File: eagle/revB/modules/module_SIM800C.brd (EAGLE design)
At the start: 24.1 x 32.8 mm, 10 parts, among them IC1 SIM800C, X1 734120110

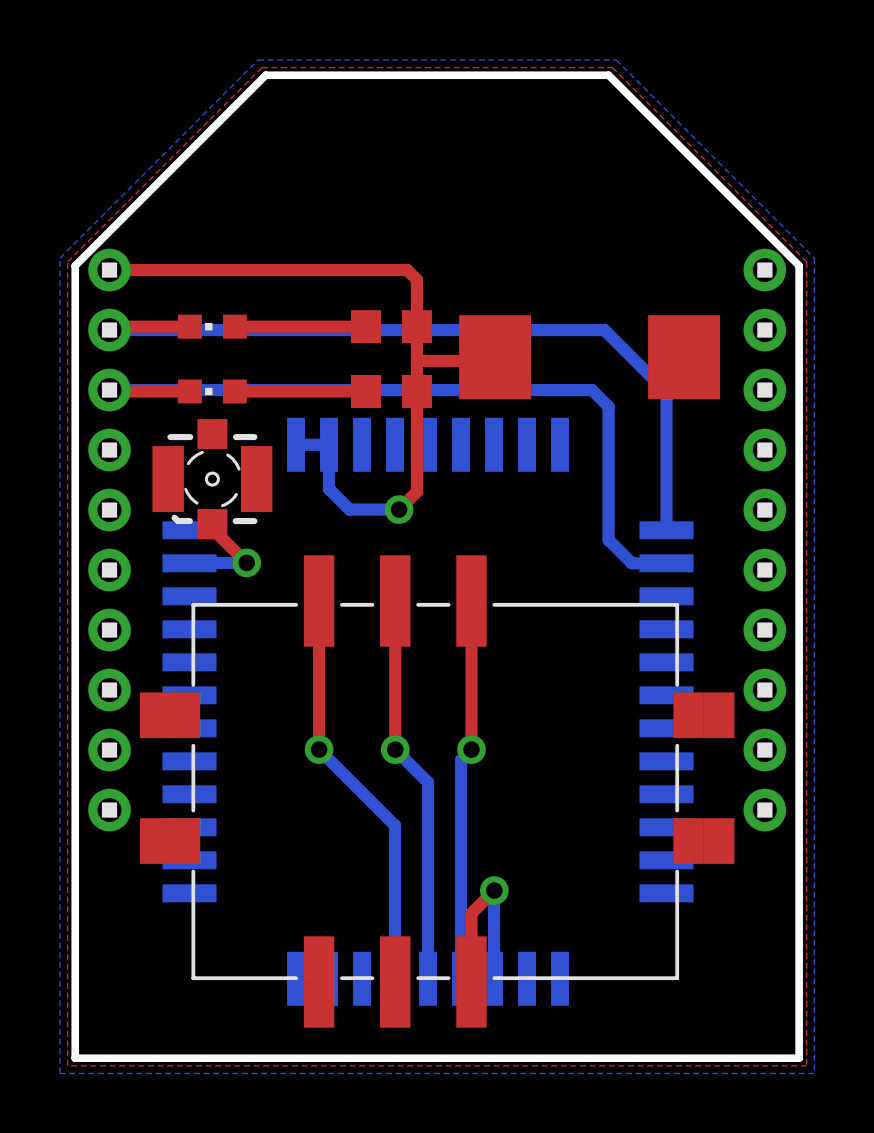
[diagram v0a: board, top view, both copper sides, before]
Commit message: [SIM800C] Updated layout
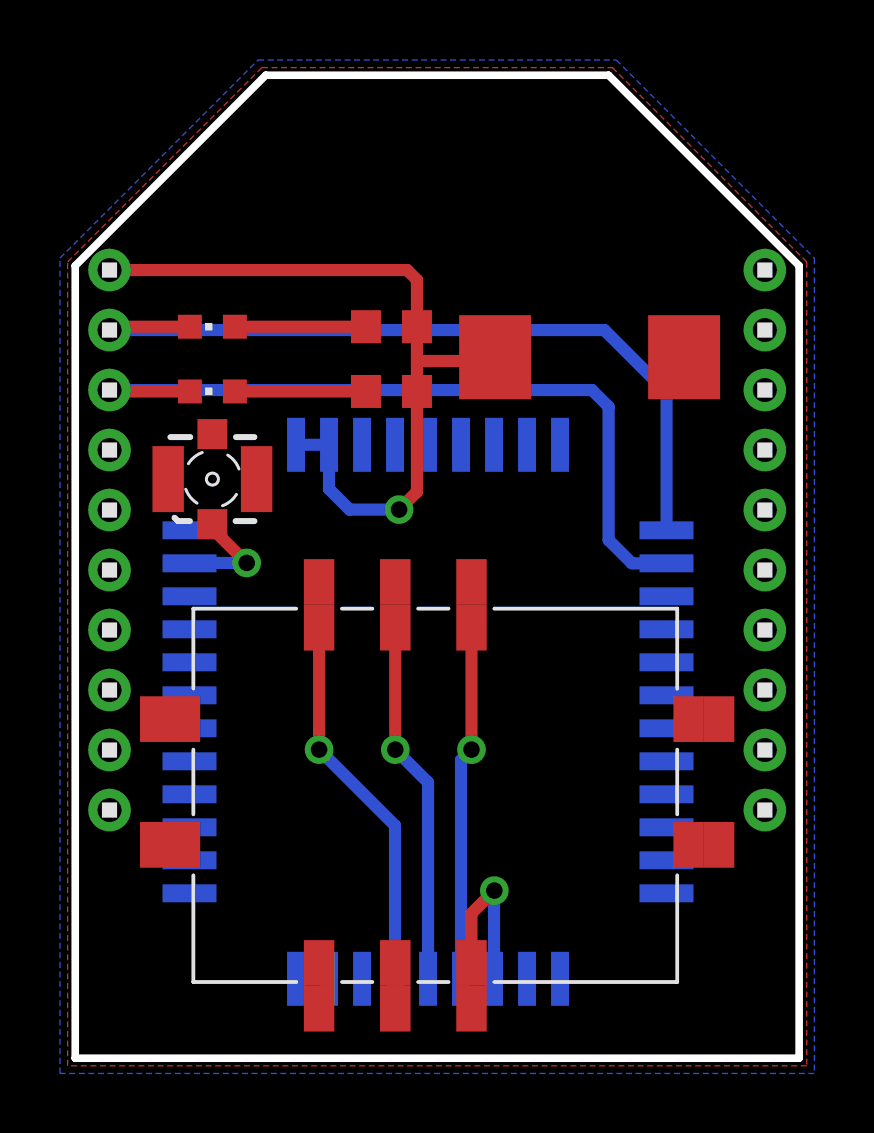
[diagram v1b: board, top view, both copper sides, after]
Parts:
- moved U$1 0.13 mm to (10.8, 8.89)
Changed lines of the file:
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@@
 <attribute name="VALUE" x="5.969" y="24.257" size="1.27" layer="27" rot="R180"/>
 </element>
-<element name="U$1" library="con-sim" package="C707-10M006-136-2" value="C707-10M006-136-2" x="10.795" y="9.017" rot="R90"/>
+<element name="U$1" library="con-sim" package="C707-10M006-136-2" value="C707-10M006-136-2" x="10.795" y="8.89" rot="R90"/>
 </elements>
 <signals>
@@
 <contactref element="IC1" pad="15"/>
 <contactref element="U$1" pad="P$3"/>
-<wire x1="13.335" y1="3.429" x2="13.335" y2="4.953" width="0.4064" layer="1"/>
+<wire x1="13.335" y1="3.302" x2="13.335" y2="4.953" width="0.4064" layer="1"/>
 <wire x1="13.335" y1="4.953" x2="14.097" y2="5.715" width="0.4064" layer="1"/>
 <via x="14.097" y="5.715" extent="1-16" drill="0.55"/>
@@
 <wire x1="12.987" y1="10.066" x2="13.335" y2="10.414" width="0.4064" layer="16"/>
 <via x="13.335" y="10.414" extent="1-16" drill="0.55"/>
-<wire x1="13.335" y1="10.414" x2="13.335" y2="14.605" width="0.4064" layer="1"/>
+<wire x1="13.335" y1="10.414" x2="13.335" y2="14.478" width="0.4064" layer="1"/>
 </signal>
 <signal name="N$6">
@@
 <wire x1="11.887" y1="9.322" x2="10.795" y2="10.414" width="0.4064" layer="16"/>
 <via x="10.795" y="10.414" extent="1-16" drill="0.55"/>
-<wire x1="10.795" y1="10.414" x2="10.795" y2="14.605" width="0.4064" layer="1"/>
+<wire x1="10.795" y1="10.414" x2="10.795" y2="14.478" width="0.4064" layer="1"/>
 </signal>
 <signal name="N$7">
@@
 <wire x1="10.787" y1="7.882" x2="8.255" y2="10.414" width="0.4064" layer="16"/>
 <via x="8.255" y="10.414" extent="1-16" drill="0.55"/>
-<wire x1="8.255" y1="10.414" x2="8.255" y2="14.605" width="0.4064" layer="1"/>
+<wire x1="8.255" y1="10.414" x2="8.255" y2="14.478" width="0.4064" layer="1"/>
 </signal>
 <signal name="VPP">
